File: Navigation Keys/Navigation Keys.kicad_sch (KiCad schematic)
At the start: 22 parts, among them J1 Conn_01x19_Female, J2 Conn_01x19_Male

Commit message: Started wiring
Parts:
- renumbered MX_Right1 to MX_Left1, MX_Left1 to MX_Right1
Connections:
- net ROW7: no longer D10.1 (K), D3.1 (K)
- net ROW8: now also D10.1 (K), D3.1 (K)
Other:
- moved on the sheet: D10, D3, MX_Left1, MX_Right1

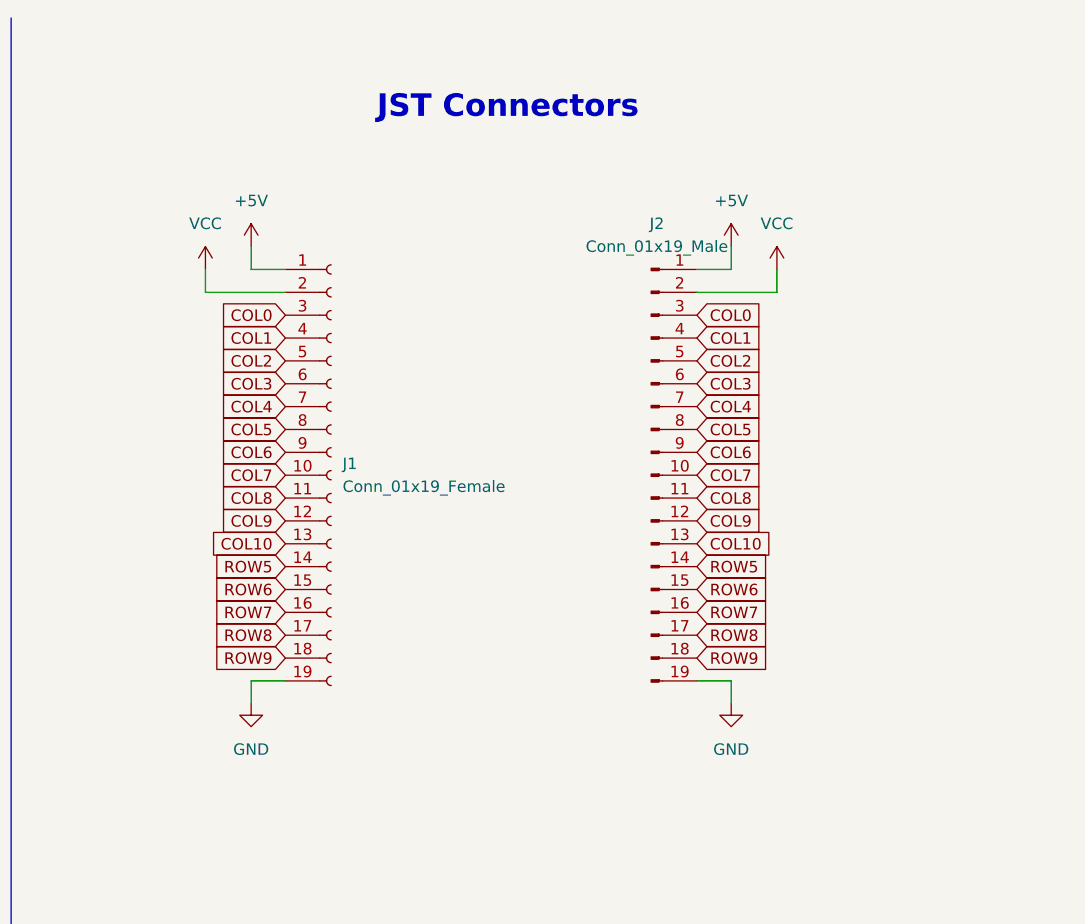
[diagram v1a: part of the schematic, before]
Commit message: Updated connectors + added mounting holes
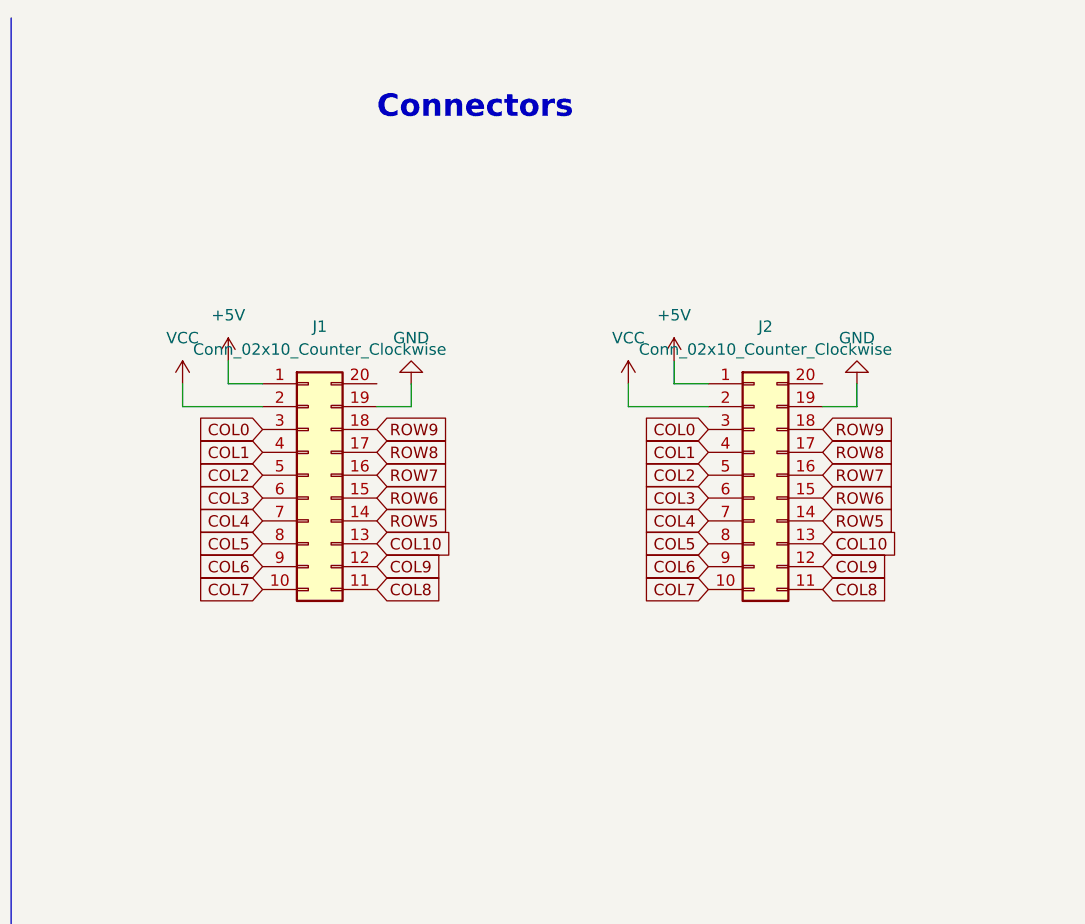
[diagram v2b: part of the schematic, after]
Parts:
- removed J1: Conn_01x19_Female, Connector_JST:JST_SH_SM20B-SRSS-TB_1x20-1MP_P1.00mm_Horizontal, symbol Connector:Conn_01x19_Female
- removed J2: Conn_01x19_Male, Connector_JST:JST_SH_SM20B-SRSS-TB_1x20-1MP_P1.00mm_Horizontal, symbol Connector:Conn_01x19_Male
- added J1: Conn_02x10_Counter_Clockwise, Connector_PinSocket_2.54mm:PinSocket_2x10_P2.54mm_Horizontal, symbol Connector_Generic:Conn_02x10_Counter_Clockwise
- added J2: Conn_02x10_Counter_Clockwise, Connector_PinHeader_2.54mm:PinHeader_2x10_P2.54mm_Horizontal, symbol Connector_Generic:Conn_02x10_Counter_Clockwise
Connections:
- net +5V: now also J1.1 (Pin_1), J2.1 (Pin_1)
- net COL0: now also J1.3 (Pin_3), J2.3 (Pin_3)
- net COL1: now also J1.4 (Pin_4), J2.4 (Pin_4)
- net COL10: now also J1.13 (Pin_13), J2.13 (Pin_13)
- net COL2: now also J1.5 (Pin_5), J2.5 (Pin_5)
- net COL3: now also J1.6 (Pin_6), J2.6 (Pin_6)
- net COL4: now also J1.7 (Pin_7), J2.7 (Pin_7)
- net COL5: now also J1.8 (Pin_8), J2.8 (Pin_8)
- net COL6: now also J1.9 (Pin_9), J2.9 (Pin_9)
- net COL7: now also J1.10 (Pin_10), J2.10 (Pin_10)
- net COL8: now also J1.11 (Pin_11), J2.11 (Pin_11)
- net COL9: now also J1.12 (Pin_12), J2.12 (Pin_12)
- net GND: now also J1.19 (Pin_19), J2.19 (Pin_19)
- net ROW5: now also J1.14 (Pin_14), J2.14 (Pin_14)
- net ROW6: now also J1.15 (Pin_15), J2.15 (Pin_15)
- net ROW7: now also J1.16 (Pin_16), J2.16 (Pin_16)
- net ROW8: now also J1.17 (Pin_17), J2.17 (Pin_17)
- net ROW9: now also J1.18 (Pin_18), J2.18 (Pin_18)
- net VCC: now also J1.2 (Pin_2), J2.2 (Pin_2)
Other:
- note added: "Connectors"
- note removed: "JST Connectors"
